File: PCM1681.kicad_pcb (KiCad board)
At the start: 2 copper layers, 88.9 x 50.8 mm, 99 parts, among them J1 USB_C_Receptacle_PowerOnly_6P, J2 Conn_01x10_Pin, J3 Conn_01x05_Pin, J4 Conn_01x05_Pin, J5 Conn_01x05_Pin, J6 AudioJack3, J7 AudioJack3, J8 AudioJack3, J9 AudioJack3, SW1 SW_DIP_x04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

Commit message: First order
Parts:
- removed J6, J7, J8, J9: AudioJack3, Connector_Audio:Jack_3.5mm_CUI_SJ-3523-SMT_Horizontal
- added J10: AudioJack4, Connector_Audio:Jack_3.5mm_PJ320D_Horizontal, F.Cu at (141.7, 31.0)
- added J11: AudioJack4, Connector_Audio:Jack_3.5mm_PJ320D_Horizontal, F.Cu at (141.9, 42.4)
- added J12: AudioJack4, Connector_Audio:Jack_3.5mm_PJ320D_Horizontal, F.Cu at (141.9, 54.9)
- added J13: \, Connector_Audio:Jack_3.5mm_PJ320D_Horizontal, F.Cu at (141.7, 65.3)
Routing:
- net /LPF1/OUT1: track 4.67 -> 7.98 mm
- net /LPF/OUT3: track 4.67 -> 7.32 mm
- net /LPF1/OUT3: track 4.67 -> 6.89 mm
- net /LPF/OUT1: track 4.67 -> 6.89 mm
- net /LPF1/OUT4: track 12.8 -> 11.4 mm
- net /LPF/OUT4: track 12.7 -> 12.2 mm
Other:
- board size 88.9 x 50.8 mm -> 83.5 x 49 mm
- board text added: "JLCJLCJLCJLC"

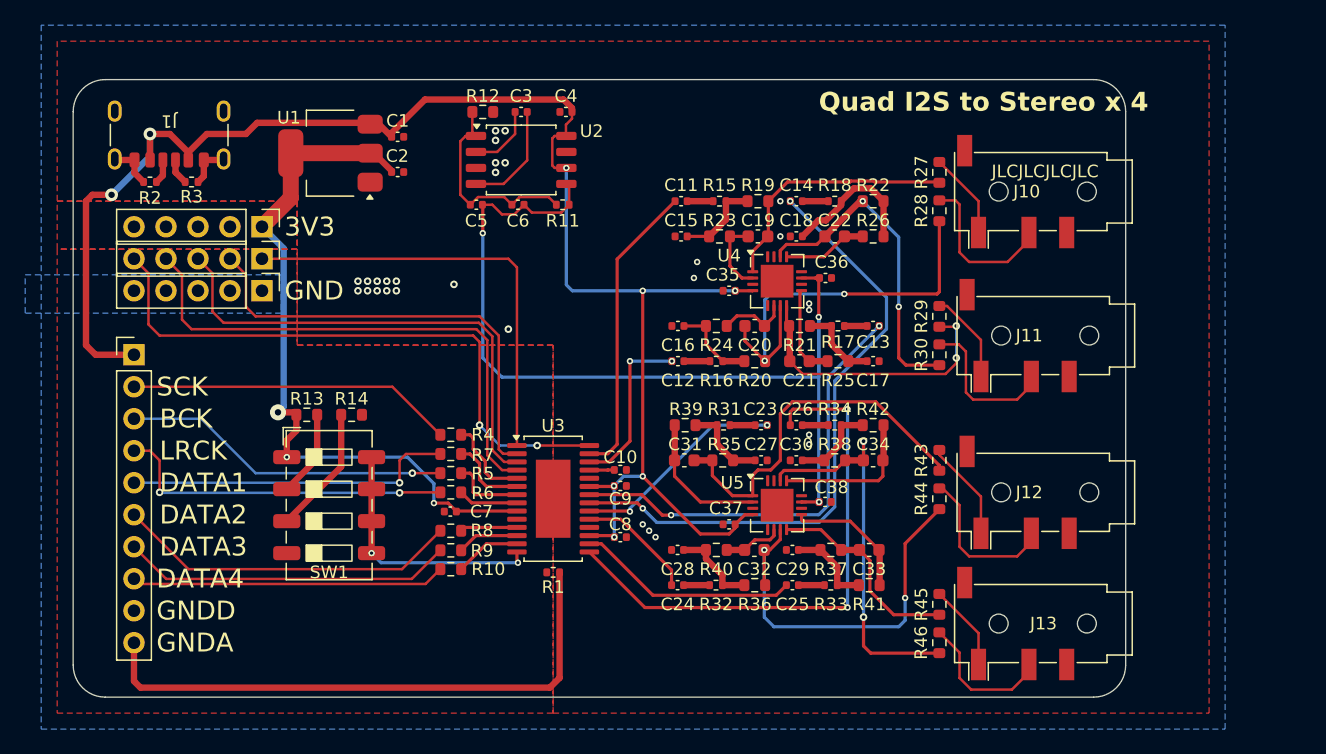
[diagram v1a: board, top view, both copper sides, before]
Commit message: Updated LCSC parts number for unmatched footprint
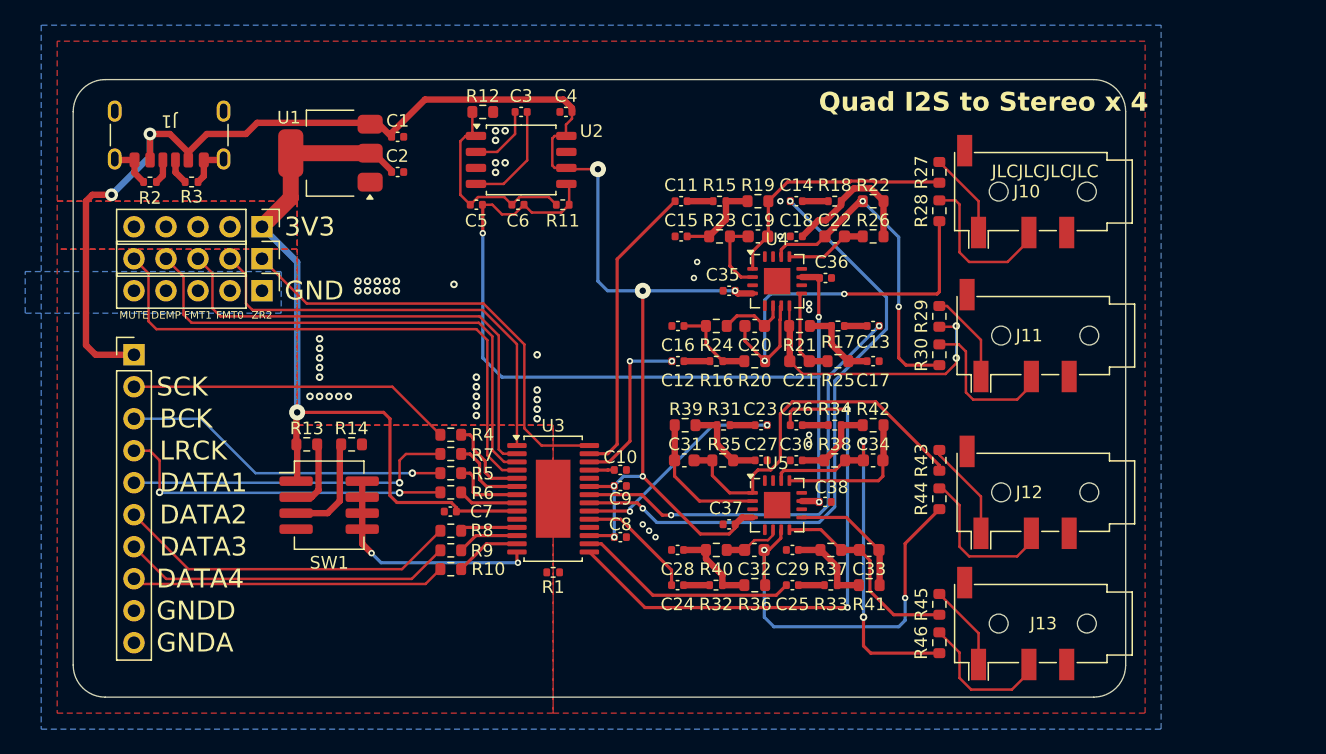
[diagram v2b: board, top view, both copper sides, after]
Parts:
- SW1: footprint Button_Switch_SMD:SW_DIP_SPSTx04_Slide_6.7x11.72mm_W6.73mm_P2.54mm_LowProfile_JPin -> Button_Switch_SMD:SW_DIP_SPSTx04_Slide_KingTek_DSHP04TJ_W5.25mm_P1.27mm_JPin
- U4, U5: footprint Package_DFN_QFN:WQFN-16-1EP_4x4mm_P0.5mm_EP2.6x2.6mm -> Package_DFN_QFN:QFN-16-1EP_4x4mm_P0.65mm_EP2.1x2.1mm
- moved R13 2.35 mm to (84.6, 51.1)
- moved R14 2.35 mm to (88.1, 51.1)
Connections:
- U3 pad 1: Net-(J5-Pin_1) -> Net-(J5-Pin_2)
- U3 pad 2: Net-(J5-Pin_2) -> Net-(J5-Pin_3)
- U3 pad 28: Net-(J5-Pin_5) -> Net-(J5-Pin_1)
- U3 pad 3: Net-(J5-Pin_3) -> Net-(J5-Pin_4)
- U3 pad 4: Net-(J5-Pin_4) -> Net-(J5-Pin_5)
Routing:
- net GNDA: track 52.9 -> 7.19 mm, vias 29 -> 48
- net +3.3V: track 58.1 -> 62.1 mm, vias 3 -> 1
- net Net-(J5-Pin_5): track 48.7 -> 44.9 mm, vias 2 -> 0
- net Net-(R14-Pad1): track 10.2 -> 8.41 mm
- net /MSEL: track 20.4 -> 18.8 mm
- net Net-(J5-Pin_1): track 34.7 -> 36.0 mm
- net Net-(R13-Pad2): track 6.90 -> 5.69 mm
- net Net-(J5-Pin_2): track 36.0 -> 35.0 mm
- net Net-(J5-Pin_4): track 42.2 -> 41.6 mm
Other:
- board text added: "DEMP"
- board text added: "FMT0"
- board text added: "FMT1"
- board text added: "MUTE"
- board text added: "ZR2"
